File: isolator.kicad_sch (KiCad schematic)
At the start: 50 parts, among them J1 HOST, J2 ISO_PORT, Q1 2N7002, T1 750313638, U1 ADuM4165, U2 USBLC6-2SC6, U3 USBLC6-2SC6, U4 SN6505BDBV, U5 TLV76750DGNR, U6 TPS2553DBV, Y1 24M 8pF

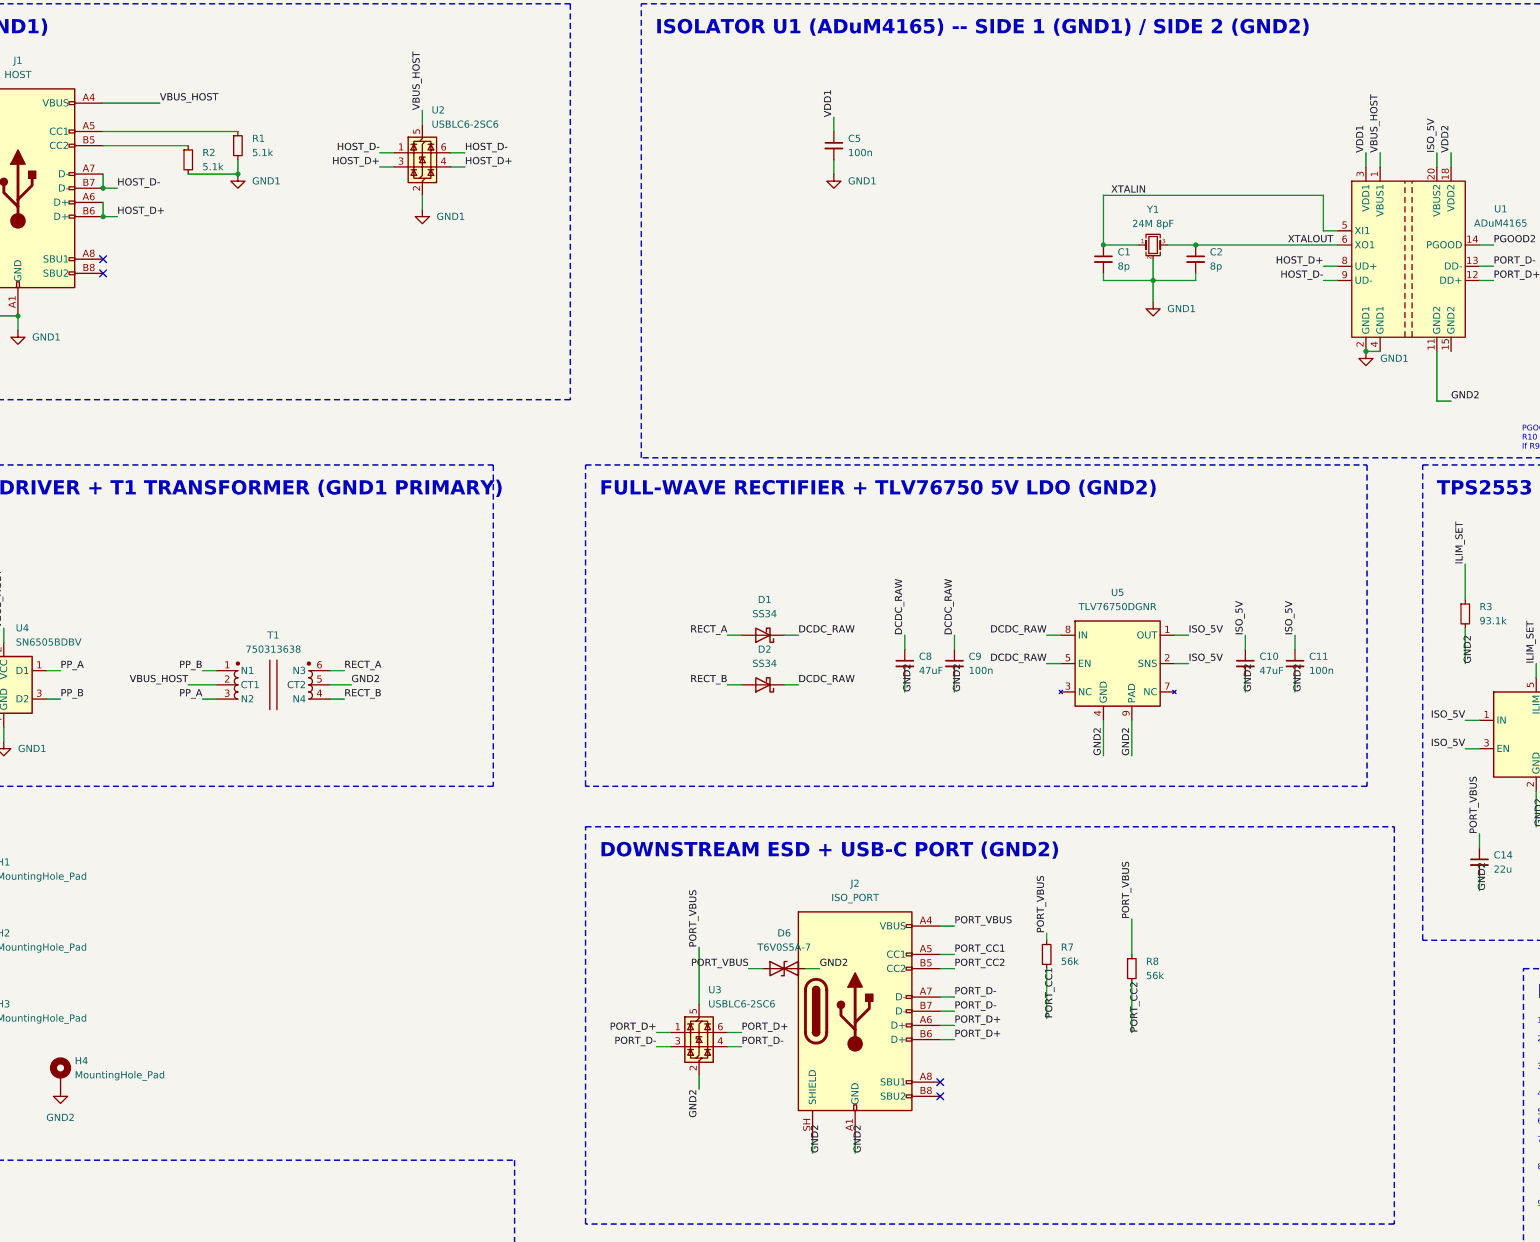
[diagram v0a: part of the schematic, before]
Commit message: feat(sch): split /DCDC_RAW into rectifier output and LDO input at NT2
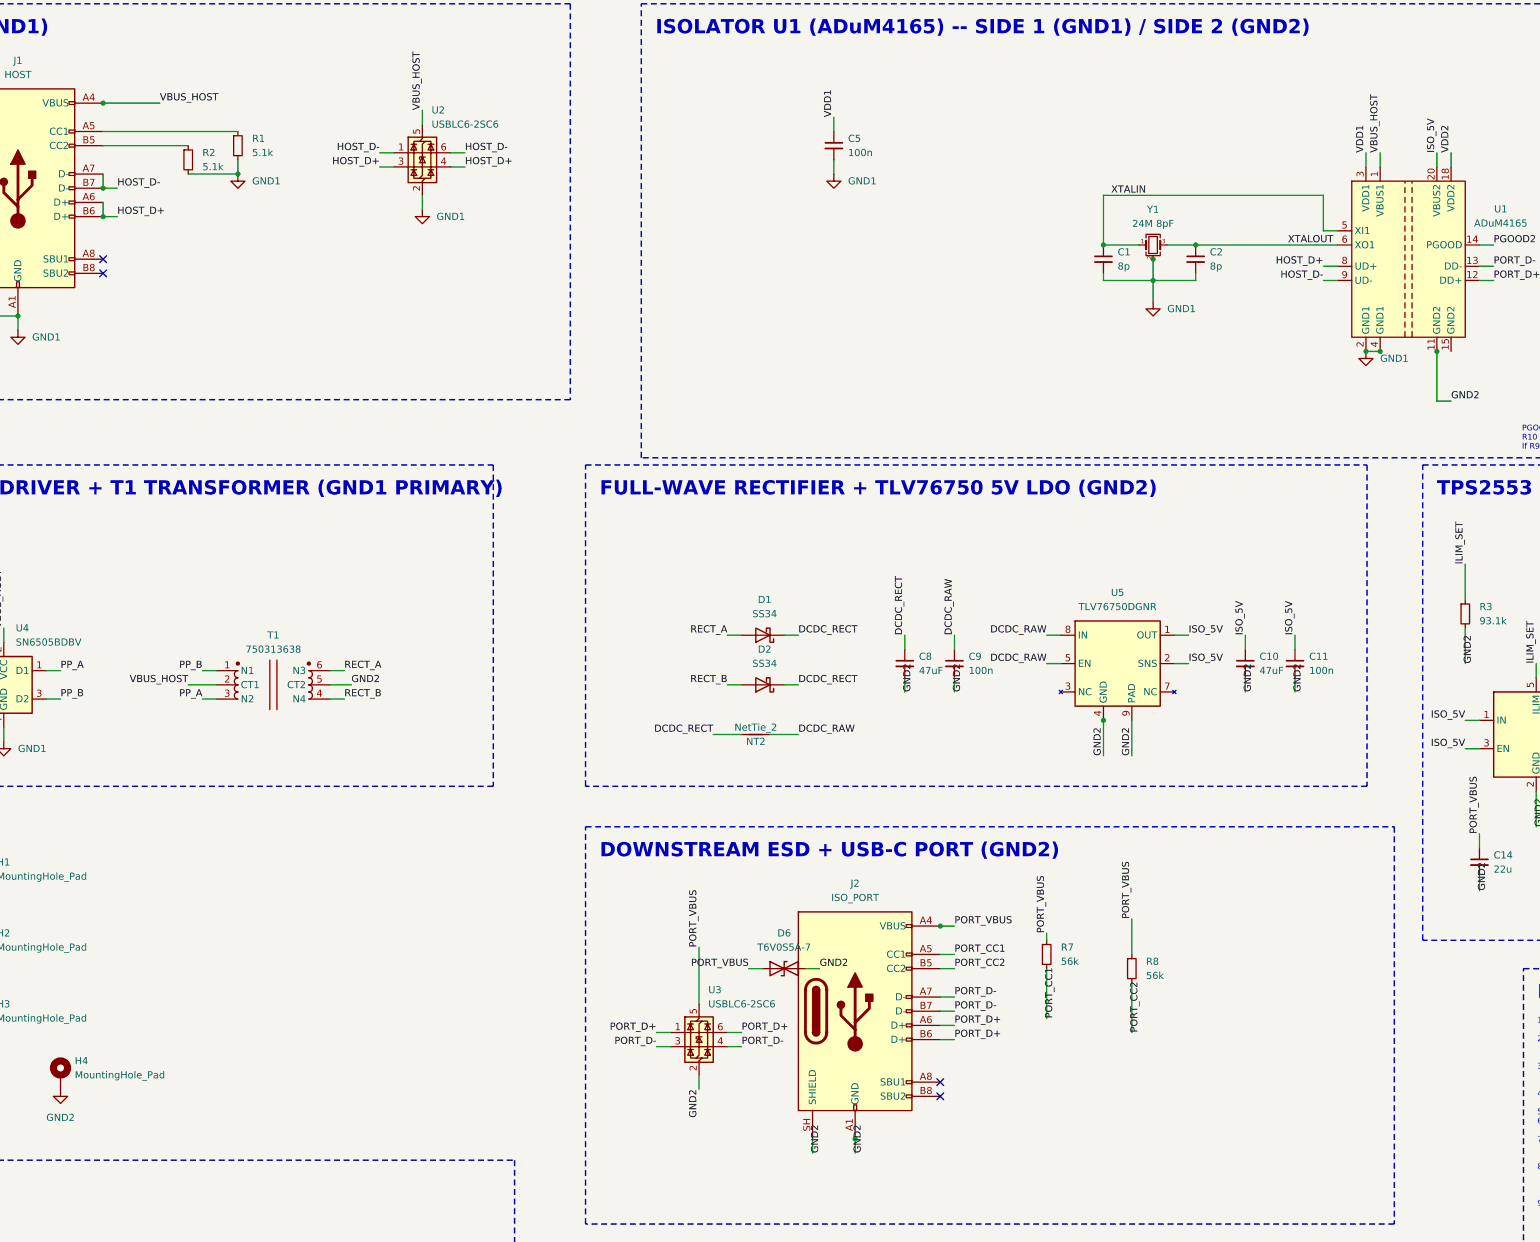
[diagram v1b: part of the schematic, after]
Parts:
- added NT2: NetTie_2, NetTie:NetTie-2_SMD_Pad0.5mm, symbol Device:NetTie_2
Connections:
- net DCDC_RAW: now also NT2.2; no longer C8.1, D1.1 (K), D2.1 (K)
- new net DCDC_RECT: C8.1, D1.1 (K), D2.1 (K), NT2.1
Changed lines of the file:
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@@
 		)
 	)
-	(label "DCDC_RAW"
+	(label "DCDC_RECT"
 		(at 203.2 130.81 0)
 		(effects
@@
 		)
 	)
-	(label "DCDC_RAW"
+	(label "DCDC_RECT"
 		(at 203.2 139.7 0)
 		(effects
@@
 		)
 	)
-	(label "DCDC_RAW"
+	(label "DCDC_RECT"
 		(at 222.25 130.81 90)
 		(effects
@@
 		)
 	)
+	(symbol
+		(lib_id "Device:NetTie_2")
+		(at 195.58 148.59 0)
+		(unit 1)
+		(body_style 1)
+		(exclude_from_sim no)
+		(in_bom yes)
+		(on_board yes)
+		(in_pos_files yes)
+		(dnp no)
+		(property "Reference" "NT2"
+			(at 195.58 149.86 0)
+			(show_name no)
+			(do_not_autoplace no)
+			(effects
+				(font
+					(size 1.27 1.27)
+				)
+			)
+		)
+		(property "Value" "NetTie_2"
+			(at 195.58 147.32 0)
+			(show_name no)
+			(do_not_autoplace no)
+			(effects
+				(font
+					(size 1.27 1.27)
+				)
+			)
+		)
+		(property "Footprint" "NetTie:NetTie-2_SMD_Pad0.5mm"
+			(at 195.58 148.59 0)
+			(hide yes)
+			(show_name no)
+			(do_not_autoplace no)
+			(effects
+				(font
+					(size 1.27 1.27)
+				)
+			)
+		)
+		(property "Datasheet" ""
+			(at 195.58 148.59 0)
+			(hide yes)
+			(show_name no)
+			(do_not_autoplace no)
+			(effects
+				(font
+					(size 1.27 1.27)
+				)
+			)
+		)
+		(property "Description" "Net tie, 2 pins"
+			(at 195.58 148.59 0)
+			(hide yes)
+			(show_name no)
+			(do_not_autoplace no)
+			(effects
+				(font
+					(size 1.27 1.27)
+				)
+			)
+		)
+		(pin "1"
+		)
+		(pin "2"
+		)
+		(instances
+			(project "isolator"
+				(path "/00000000-0000-0000-0000-000000000001"
+					(reference "NT2")
+					(unit 1)
+				)
+			)
+		)
+	)
+	(wire
+		(pts
+			(xy 193.04000000000002 148.59) (xy 187.96 148.59)
+		)
+		(stroke
+			(width 0)
+			(type default)
+		)
+	)
+	(junction
+		(at 213.36 220.98)
+		(diameter 0)
+		(color 0 0 0 0)
+	)
+	(junction
+		(at 307.34 80.01)
+		(diameter 0)
+		(color 0 0 0 0)
+	)
+	(junction
+		(at 78.74 35.56)
+		(diameter 0)
+		(color 0 0 0 0)
+	)
+	(junction
+		(at 266.7 63.5)
+		(diameter 0)
+		(color 0 0 0 0)
+	)
+	(junction
+		(at 228.6 182.88)
+		(diameter 0)
+		(color 0 0 0 0)
+	)
+	(junction
+		(at 317.5 80.01)
+		(diameter 0)
+		(color 0 0 0 0)
+	)
+	(junction
+		(at 257.81 146.05)
+		(diameter 0)
+		(color 0 0 0 0)
+	)
+	(wire
+		(pts
+			(xy 198.12 148.59) (xy 203.2 148.59)
+		)
+		(stroke
+			(width 0)
+			(type default)
+		)
+	)
+	(label "DCDC_RECT"
+		(at 187.96 148.59 180)
+		(effects
+			(font
+				(size 1.27 1.27)
+			)
+			(justify right bottom)
+		)
+	)
+	(label "DCDC_RAW"
+		(at 203.2 148.59 0)
+		(effects
+			(font
+				(size 1.27 1.27)
+			)
+			(justify left bottom)
+		)
+	)

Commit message: fix(sch): NT2 net tie must not appear in BOM
in_bom yes on the placed NT2 instance overrode the Device:NetTie_2
library default of in_bom no. Task 5's BOM acceptance check requires
NT1-NT3 absent from isolator-bom.csv.
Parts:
- NT2: now left out of the parts list
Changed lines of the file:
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@@
 		(body_style 1)
 		(exclude_from_sim no)
-		(in_bom yes)
+		(in_bom no)
 		(on_board yes)
 		(in_pos_files yes)

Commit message: feat(sch): split /PORT_VBUS into switch output and connector at NT3
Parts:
- added NT3: NetTie_2, NetTie:NetTie-2_SMD_Pad0.5mm, symbol Device:NetTie_2
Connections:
- net PORT_VBUS: now also NT3.1; no longer D6.1 (A1), J2.A4 (VBUS), J2.A9 (VBUS), J2.B4 (VBUS), J2.B9 (VBUS), R7.1, R8.1, U3.5 (VBUS)
- new net PORT_VBUS_J2: D6.1 (A1), J2.A4 (VBUS), J2.A9 (VBUS), J2.B4 (VBUS), J2.B9 (VBUS), NT3.2, R7.1, R8.1, U3.5 (VBUS)
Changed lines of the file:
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@@
 		)
 	)
-	(label "PORT_VBUS"
+	(label "PORT_VBUS_J2"
 		(at 185.42 186.69 90)
 		(effects
@@
 		)
 	)
-	(label "PORT_VBUS"
+	(label "PORT_VBUS_J2"
 		(at 262.89 181.61 90)
 		(effects
@@
 		)
 	)
-	(label "PORT_VBUS"
+	(label "PORT_VBUS_J2"
 		(at 231.14 182.88 0)
 		(effects
@@
 		)
 	)
-	(label "PORT_VBUS"
+	(label "PORT_VBUS_J2"
 		(at 247.65 184.15 90)
 		(effects
@@
 		)
 	)
-	(label "PORT_VBUS"
+	(label "PORT_VBUS_J2"
 		(at 194.31 190.5 180)
 		(effects
@@
 		(effects
 			(font
+				(size 1.27 1.27)
+			)
+			(justify left bottom)
+		)
+	)
+	(symbol
+		(lib_id "Device:NetTie_2")
+		(at 365.76 163.83 0)
+		(unit 1)
+		(body_style 1)
+		(exclude_from_sim no)
+		(in_bom no)
+		(on_board yes)
+		(in_pos_files yes)
+		(dnp no)
+		(property "Reference" "NT3"
+			(at 365.76 165.1 0)
+			(show_name no)
+			(do_not_autoplace no)
+			(effects
+				(font
+					(size 1.27 1.27)
+				)
+			)
+		)
+		(property "Value" "NetTie_2"
+			(at 365.76 162.56 0)
+			(show_name no)
+			(do_not_autoplace no)
+			(effects
+				(font
+					(size 1.27 1.27)
+				)
+			)
+		)
+		(property "Footprint" "NetTie:NetTie-2_SMD_Pad0.5mm"
+			(at 365.76 163.83 0)
+			(hide yes)
+			(show_name no)
+			(do_not_autoplace no)
+			(effects
+				(font
+					(size 1.27 1.27)
+				)
+			)
+		)
+		(property "Datasheet" ""
+			(at 365.76 163.83 0)
+			(hide yes)
+			(show_name no)
+			(do_not_autoplace no)
+			(effects
+				(font
+					(size 1.27 1.27)
+				)
+			)
+		)
+		(property "Description" "Net tie, 2 pins"
+			(at 365.76 163.83 0)
+			(hide yes)
+			(show_name no)
+			(do_not_autoplace no)
+			(effects
+				(font
+					(size 1.27 1.27)
+				)
+			)
+		)
+		(pin "1"
+		)
+		(pin "2"
+		)
+		(instances
+			(project "isolator"
+				(path "/00000000-0000-0000-0000-000000000001"
+					(reference "NT3")
+					(unit 1)
+				)
+			)
+		)
+	)
+	(wire
+		(pts
+			(xy 363.21999999999997 163.83) (xy 358.14 163.83)
+		)
+		(stroke
+			(width 0)
+			(type default)
+		)
+	)
+	(wire
+		(pts
+			(xy 368.3 163.83) (xy 373.38 163.83)
+		)
+		(stroke
+			(width 0)
+			(type default)
+		)
+	)
+	(label "PORT_VBUS"
+		(at 358.14 163.83 180)
+		(effects
+			(font
+				(size 1.27 1.27)
+			)
+			(justify right bottom)
+		)
+	)
+	(label "PORT_VBUS_J2"
+		(at 373.38 163.83 0)
+		(effects
+			(font

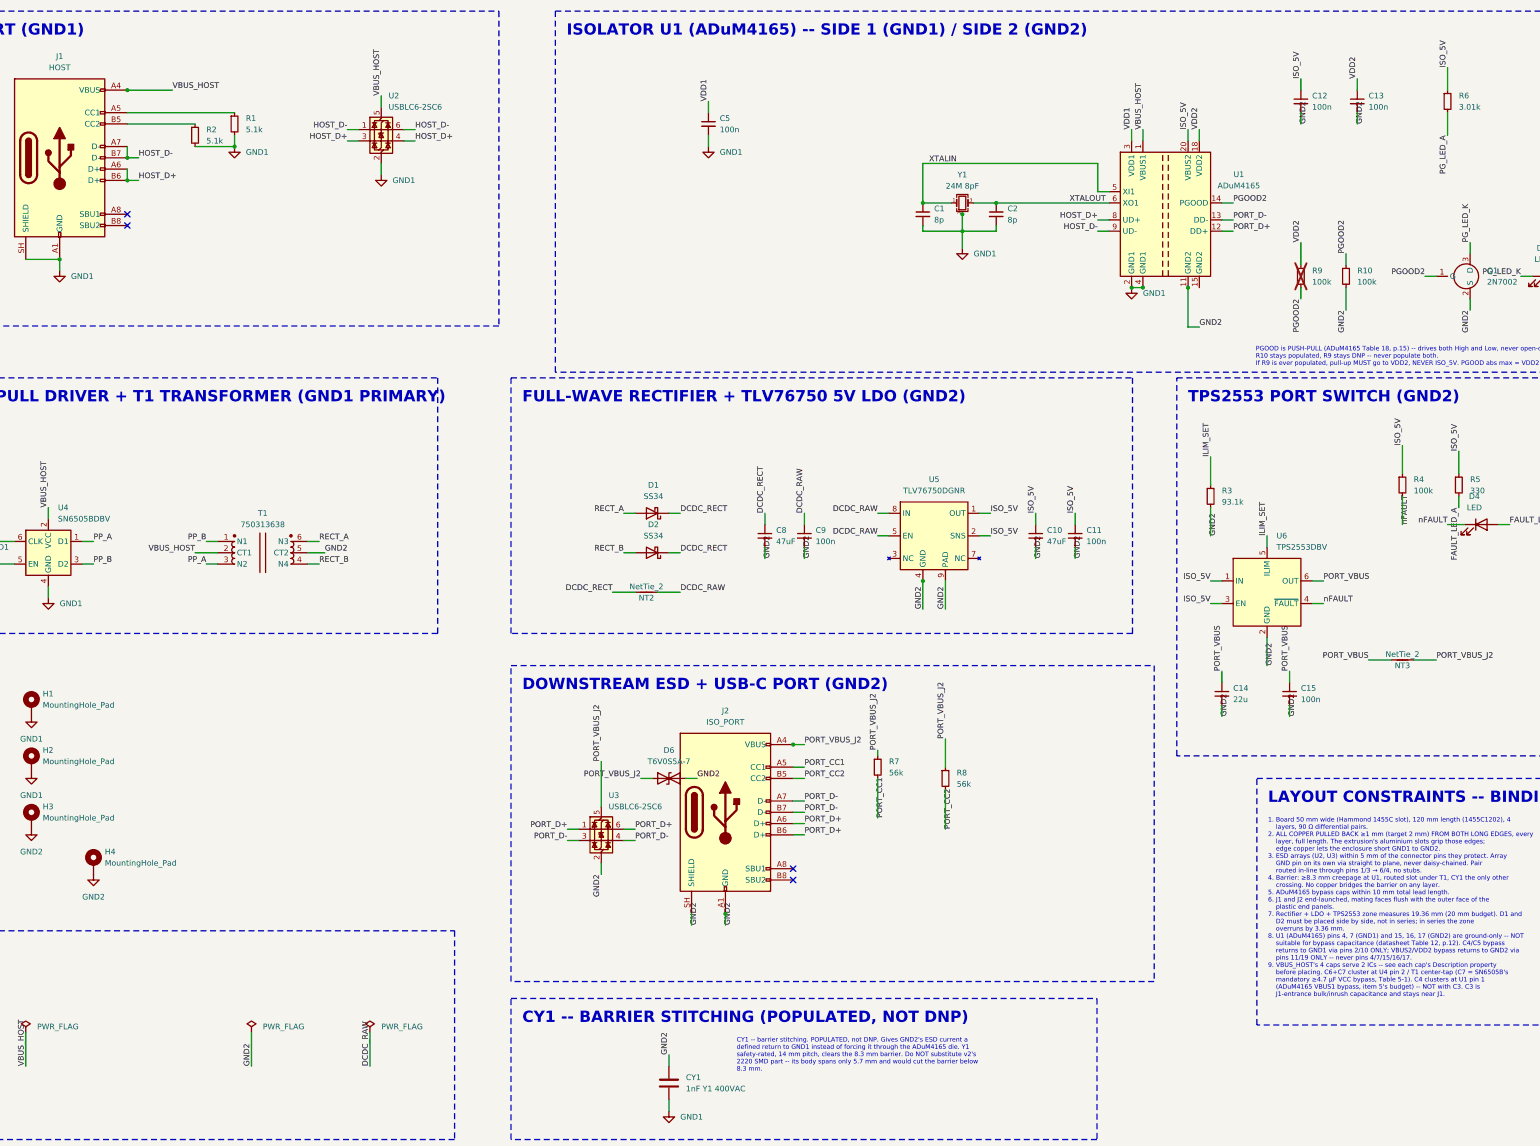
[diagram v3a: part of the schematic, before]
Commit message: feat(sch): split /ISO_5V into LDO, VBUS2, switch and indicator branches at NT1
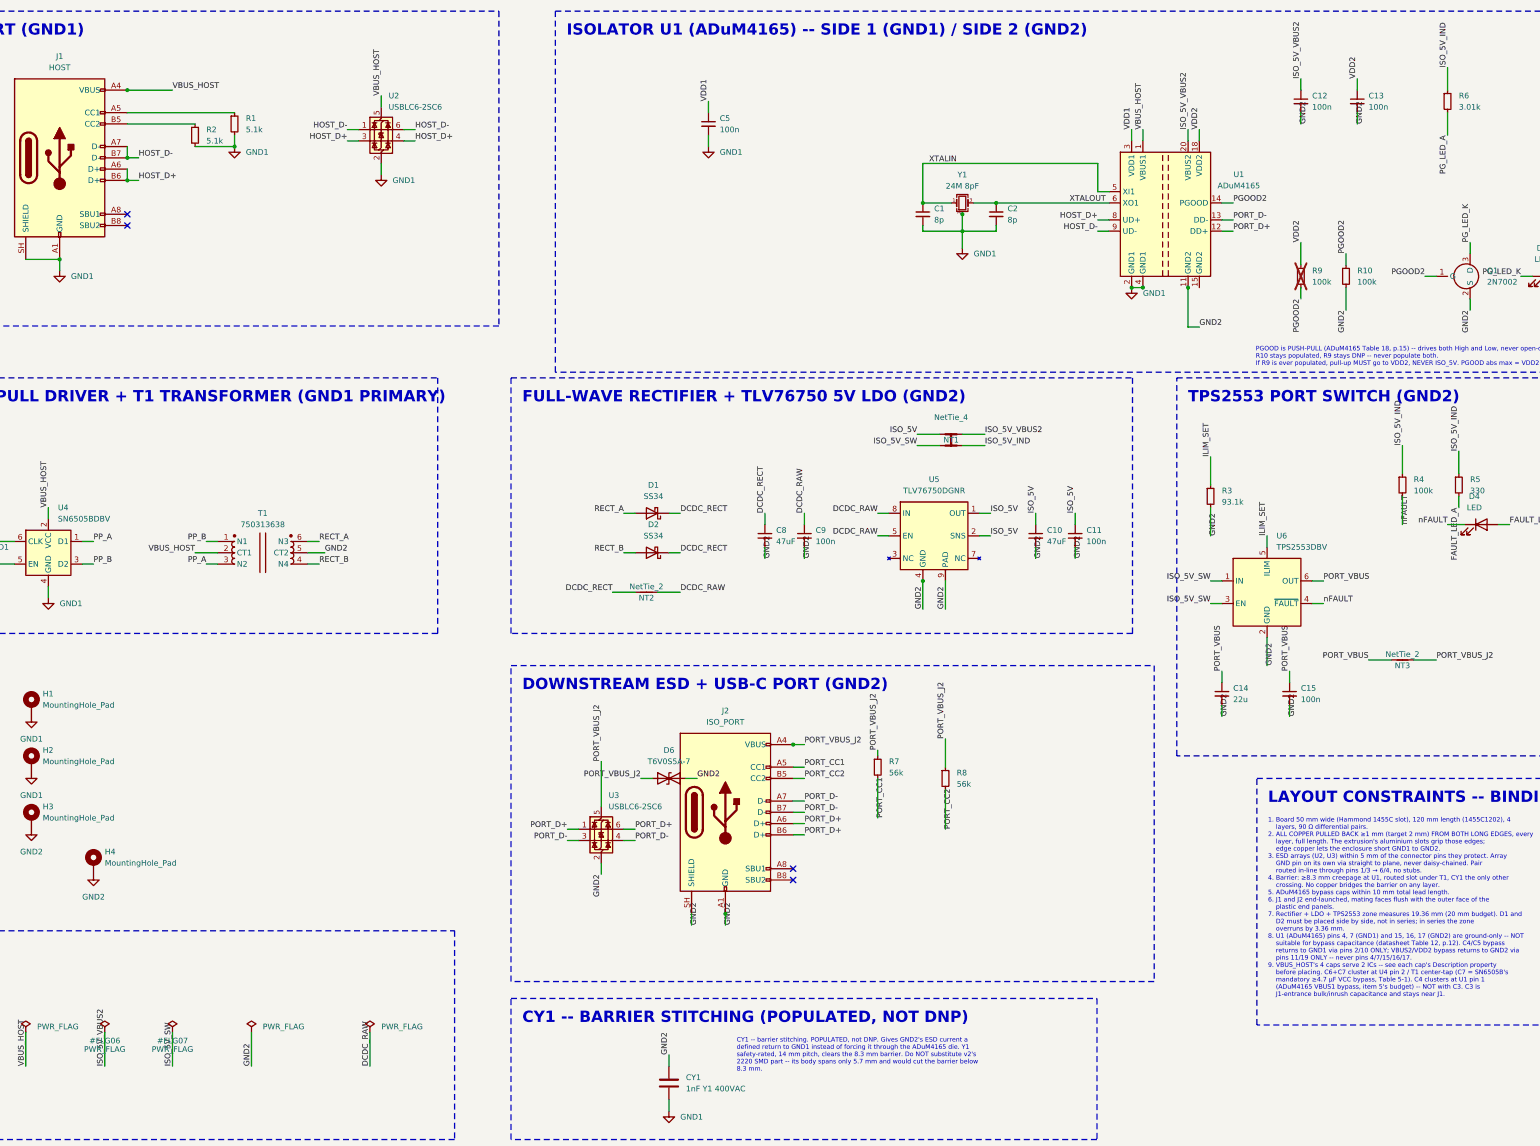
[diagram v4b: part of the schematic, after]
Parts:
- added NT1: NetTie_4, NetTie:NetTie-4_SMD_Pad0.5mm, symbol Device:NetTie_4
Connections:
- net ISO_5V: now also NT1.1; no longer C12.1, R4.1, R5.1, R6.1, U1.20 (VBUS2), U6.1 (IN), U6.3 (EN)
- new net ISO_5V_IND: NT1.4, R4.1, R5.1, R6.1
- new net ISO_5V_SW: NT1.3, U6.1 (IN), U6.3 (EN)
- new net ISO_5V_VBUS2: C12.1, NT1.2, U1.20 (VBUS2)
